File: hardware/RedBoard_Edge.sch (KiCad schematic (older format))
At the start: 67 parts, among them IC3 LM1117, J1 CONN_025MM, J17 Qwiic_Connector, J18 Qwiic_Connector, J2 ICSP, J3 POWER_JACKSUPER_BOMB_DIGITY, J4 microB, J5 CONN_04, J6 CONN_04, Q1 1A/60V/500mO, Q2 MOSFET-NCH-BSS138, Q3 MOSFET-NCH-BSS138, U1 CH340G, U2 MIC5205, U3 Standoff_Grounding, U4 ATMEGA328P_TQFP, U5 Standoff_Grounding, Y1 16MHz, Y2 12MHz

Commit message: conversion to Reds, all parts now point to KiCad library in directory C:/Github
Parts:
- removed C1, C2, C4, C8: 0.1uF, RedBoard:SPARKFUN-CAPACITORS_0603, symbol SPARKFUN-CAPACITORS_0.1UF-0603-25V-_+80_-20%_
- removed C10, C9: 10pF, Capacitors_SMD:C_0603, symbol C_Small
- removed C11: 10nF, Capacitors_SMD:C_0603, symbol C_Small
- removed C12: 0.1uF, Capacitors_SMD:C_0603, symbol C_Small
- removed C3, C6: 10uF, RedBoard:SPARKFUN-CAPACITORS_EIA3216, symbol SPARKFUN-CAPACITORS_10UF-POLAR-EIA3216-16V-10%_TANT_
- removed C5: 47uF, RedBoard:SPARKFUN-CAPACITORS_PANASONIC_D, symbol SPARKFUN-CAPACITORS_47UF-POLAR-PANASONIC_D-35V-20%
- removed C7: 1.0uF, RedBoard:SPARKFUN-CAPACITORS_0603, symbol SPARKFUN-CAPACITORS_1.0UF-0603-16V-10%
- removed D1: MBRA140, RedBoard:SPARKFUN-DISCRETESEMI_SMA-DIODE, symbol SPARKFUN-DISCRETESEMI_MBRA140
- removed D2: Green, NewParts:LED_RED_T1-.75_RT_ANG_PCB, symbol SPARKFUN-LED_LED-GREEN0603
- removed D3: Yellow, NewParts:LED_RED_T1-.75_RT_ANG_PCB, symbol SPARKFUN-LED_LED-YELLOW0603
- removed D4: Red, NewParts:LED_RED_T1-.75_RT_ANG_PCB, symbol SPARKFUN-LED_LED-YELLOW0603
- removed D5: Blue, NewParts:LED_RED_T1-.75_RT_ANG_PCB, symbol SPARKFUN-LED_LED-YELLOW0603
- removed F1: SPARKFUN-FUSES_PTC-HALF_AMP, RedBoard:SPARKFUN-FUSES_1206, symbol SPARKFUN-FUSES_PTC-HALF_AMP
- removed IC3: LM1117, RedBoard:TESTING_SOT223-ALT1, symbol TESTING_V_REG_LM1117ALT1
- removed J17, J18: Qwiic_Connector, SparkX:SparkX-1X04_1MM_RA, symbol Qwiic_Connector
- removed J2: ICSP, RedBoard:SPARKFUN-CONNECTORS_2X3_SMT_POSTS, symbol SPARKFUN-CONNECTORS_AVR_SPI_PROG_3X2SMD
- removed J3: POWER_JACKSUPER_BOMB_DIGITY, RedBoard:TESTING_POWER_JACK_SMD_OVERPASTE_SUPER_BOMB_DIGITY, symbol TESTING_POWER_JACKSUPER_BOMB_DIGITY
- removed J4: microB, Connectors:USB-B-MICRO-SMD, symbol microB
- removed JP1, JP2: JUMPER-SMT_2_NO_SILK, Jumpers:SMT-JUMPER_2_NO_SILK, symbol JUMPER-SMT_2_NO_SILK
- removed JP4, JP6: STAND-OFF, RedBoard:SPARKFUN_STAND-OFF, symbol SPARKFUN_STAND-OFF
- removed JP8, JP9: FIDUCIAL1X2, RedBoard:SPARKFUN_FIDUCIAL-1X2, symbol SPARKFUN_FIDUCIAL1X2
- removed Q1: 1A/60V/500mO, RedBoard:SPARKFUN-DISCRETESEMI_SOT23-3, symbol SPARKFUN-DISCRETESEMI_MOSFET-PCH-ZXMP6A13F
- removed R1: 1k, RedBoard:SPARKFUN-RESISTORS_0603, symbol SPARKFUN-RESISTORS_1KOHM-0603-1_10W-1%
- removed R10, R7, R8, R9: 4.7k, RedBoard:SPARKFUN-RESISTORS_0603, symbol SPARKFUN-RESISTORS_10KOHM-0603-1_10W-1%
- removed R14: 715, RedBoard:SPARKFUN-RESISTORS_0603, symbol SPARKFUN-RESISTORS_715OHM-0603-1_10W-1%
- removed R15: 240, RedBoard:SPARKFUN-RESISTORS_0603, symbol SPARKFUN-RESISTORS_240OHM-0603-1_10W-1%
- removed R2: 1k, RedBoard:SPARKFUN-RESISTORS_0603, symbol SPARKFUN-RESISTORS_4.7KOHM-0603-1_10W-1%
- removed R3, R4: 10k, RedBoard:SPARKFUN-RESISTORS_0603, symbol SPARKFUN-RESISTORS_10KOHM-0603-1_10W-1%
- removed R5, R6: 1k, RedBoard:SPARKFUN-RESISTORS_0603, symbol R_Small
- removed S1: RESET, NewParts:SWITCH_TACTILE_SPST-NO_0.05A_12V, symbol SPARKFUN-ELECTROMECHANICAL_SWITCH_SPST_4_PINSQUARE
- removed S2: SWITCH-SPDT-PTH-11.6X4.0MM, NewParts:RockerSwitch_RA, symbol SWITCH-SPDT-PTH-11.6X4.0MM
- removed U$1: SPARKX-LOGO5, SparkX:SparkX-SPARKX-LARGE, symbol SPARKX_SPARKX-LOGO5
- removed U1: CH340G, IC:SO16, symbol SPARKFUN-DIGITALIC_CH340GSMD
- removed U2: MIC5205, RedBoard:SPARKFUN-POWERIC_SOT23-5, symbol SPARKFUN-POWERIC_MIC52053.3V
- removed U4: ATMEGA328P_TQFP, RedBoard:SPARKFUN-IC-MICROCONTROLLER_TQFP32-08, symbol SPARKFUN-IC-MICROCONTROLLER_ATMEGA328P_TQFP
- removed Y1: 16MHz, RedBoard:SPARKFUN-CLOCKS_RESONATOR-SMD-3.2X1.3, symbol SPARKFUN-CLOCKS_RESONATOR-16MHZSMD_3.2X1.3
- removed Y2: 12MHz, Clocks:CRYSTAL-SMD-3.2X2.5MM, symbol CRYSTAL-GROUNDED
- added C1, C12, C2, C4, C8: 0.1UF-0603-25V-_+80_-20%_, 0603, symbol 0.1UF-0603-25V-_+80_-20%_
- added C10, C9: 10PF-0603-50V-5%, 0603, symbol 10PF-0603-50V-5%
- added C11: 10NF-0603-50V-10%, 0603, symbol 10NF-0603-50V-10%
- added C3, C6: 10UF-POLAR-EIA3216-16V-10%_TANT_, EIA3216, symbol 10UF-POLAR-EIA3216-16V-10%_TANT_
- added C5: 47UF-POLAR-EIA3528-10V-10%, EIA3528, symbol 47UF-POLAR-EIA3528-10V-10%
- added C7: 1.0UF-0603-16V-10%, 0603, symbol 1.0UF-0603-16V-10%
- added D1: DIODE-SHOTTKY_MBRA140, Silicon-Standard:SMA-DIODE, symbol DIODE-SHOTTKY_MBRA140
- added D2, D5: SPARKFUN-LED_LED-YELLOW-550, LED:LED_550_T1-.75_RT_ANG_PCB, symbol SPARKFUN-LED_LED-YELLOW-550
- added D3: SPARKFUN-LED_LED-GREEN-550, LED:LED_550_T1-.75_RT_ANG_PCB, symbol SPARKFUN-LED_LED-GREEN-550
- added D4: SPARKFUN-LED_LED-RED-550, LED:LED_550_T1-.75_RT_ANG_PCB, symbol SPARKFUN-LED_LED-RED-550
- added F1: PPTC_HALF-AMP, 1206, symbol PPTC_HALF-AMP
- added FD1, FD2, FD3, FD4: FIDUCIAL1X2, FIDUCIAL-1X2, symbol FIDUCIAL1X2
- added H1, H2: STAND-OFF, STAND-OFF, symbol STAND-OFF
- added J17, J18: QWIIC_CONNECTORJS-1MM, 1X04_1MM_RA, symbol QWIIC_CONNECTORJS-1MM
- added J2: CONN_03X2SMT, 2X3_SMT_POSTS, symbol CONN_03X2SMT
- added J20: POWER_JACKSMD, POWER_JACK_SMD, symbol POWER_JACKSMD
- added J4: USB_MICRO-B_FEMALE-SMT, USB-B-MICRO-SMD, symbol USB_MICRO-B_FEMALE-SMT
- added JP1, JP2: JUMPER-SMT_2_NO, SMT-JUMPER_2_NO, symbol JUMPER-SMT_2_NO
- added LOGO?: SPARKFUN-AESTHETICS_SFE_LOGO_NAME.1_INCH, symbol SPARKFUN-AESTHETICS_SFE_LOGO_NAME.1_INCH
- added Q1: MOSFET_PCH-SI2309DS, SOT23-3, symbol MOSFET_PCH-SI2309DS
- added R1, R2, R5, R6: 470OHM-0603-1_10W-1%, 0603, symbol 470OHM-0603-1_10W-1%
- added R10, R7, R8, R9: 4.7KOHM-0603-1_10W-1%, 0603, symbol 4.7KOHM-0603-1_10W-1%
- added R14: 715OHM-0603-1_10W-1%, 0603, symbol 715OHM-0603-1_10W-1%
- added R15: 240OHM-0603-1_10W-1%, 0603, symbol 240OHM-0603-1_10W-1%
- added R3, R4: 10KOHM-0603-1_10W-1%, 0603, symbol 10KOHM-0603-1_10W-1%
- added S1: MOMENTARY-SWITCH-SPST-2-PTH-RT-ANGLE, Switches:TACTILE_SWITCH_PTH_RIGHT_ANGLE_KIT, symbol MOMENTARY-SWITCH-SPST-2-PTH-RT-ANGLE
- added S2: ROCKER_SWITCH-SPST_PTH_RIGHT_ANGLE, TACTILE_SWITCH_SMD_RIGHT_ANGLE, symbol ROCKER_SWITCH-SPST_PTH_RIGHT_ANGLE
- added U1: CH340GSMD, Silicon-Standard:SO16, symbol CH340GSMD
- added U2: V_REG_MIC52053.3V, SOT23-5, symbol V_REG_MIC52053.3V
- added U4: ATMEGA328P_TQFP, TQFP32-08, symbol ATMEGA328P_TQFP
- added U6: V_REG_LM1117SOT223, SOT223, symbol V_REG_LM1117SOT223
- added Y1: RESONATOR-16MHZSMD_3.2X1.3, RESONATOR-SMD-3.2X1.3, symbol RESONATOR-16MHZSMD_3.2X1.3
- added Y2: CRYSTAL-12MHZ\", CRYSTAL-SMD-5X3.2-4PAD, symbol CRYSTAL-12MHZ"
- 5V1, ADC1, GND1: footprint Connectors:1X06 -> 1X06; Field4 (none) -> CONN-08437
- 5V2, 5V3, GND2, GND3, J5, J6, PWM1, SPI1: footprint Connectors:1X04 -> 1X04; Field4 (none) -> CONN-09696
- J1: footprint Connectors:SCREWTERMINAL-5MM-2 -> SCREWTERMINAL-5MM-2; Field4 (none) -> PRT-08432
- Q2, Q3: footprint DiscreteSemi:SparkFun-DiscreteSemi-SOT23-3 -> SOT23-3; Field4 (none) -> TRANS-00830
- U3, U5: footprint NewParts:Standoff_Grounding -> Hardware:STANDOFF_GROUNDING
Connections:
- wire segments 250 -> 246

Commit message: Conversion to Reds
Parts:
- added J3, J7, J8: CONN_02, symbol CONN_02
- 5V1, ADC1, GND1: footprint 1X06 -> (none)
- 5V2, 5V3, GND2, GND3, J5, J6, PWM1, SPI1: footprint 1X04 -> (none)
- C1, C10, C11, C12, C2, C4, C7, C8, C9: footprint 0603 -> Capacitors:0603
- C3, C6: footprint EIA3216 -> Capacitors:EIA3216
- C5: footprint EIA3528 -> Capacitors:EIA3528
- F1: footprint 1206 -> Fuses:1206
- FD1, FD2, FD3, FD4: footprint FIDUCIAL-1X2 -> Aesthetics:FIDUCIAL-MICRO
- H1, H2: footprint STAND-OFF -> Hardware:STAND-OFF-TIGHT
- J1: footprint SCREWTERMINAL-5MM-2 -> (none)
- J17, J18: footprint 1X04_1MM_RA -> (none)
- J2: footprint 2X3_SMT_POSTS -> (none)
- J20: footprint POWER_JACK_SMD -> (none)
- J4: footprint USB-B-MICRO-SMD -> (none)
- JP1, JP2: footprint SMT-JUMPER_2_NO -> Jumpers:SMT-JUMPER_2_NO_NO-SILK
- Q1, Q2, Q3: footprint SOT23-3 -> Silicon-Standard:SOT23-3
- R1, R10, R14, R15, R2, R3, R4, R5, R6, R7, R8, R9: footprint 0603 -> Resistors:0603
- S2: footprint TACTILE_SWITCH_SMD_RIGHT_ANGLE -> Switches:TACTILE_SWITCH_SMD_RIGHT_ANGLE
- U2: footprint SOT23-5 -> Silicon-Standard:SOT23-5
- U4: footprint TQFP32-08 -> Silicon-Standard:TQFP32-08
- U6: footprint SOT223 -> Silicon-Standard:SOT223
- Y1: footprint RESONATOR-SMD-3.2X1.3 -> Clocks:RESONATOR-SMD-3.2X1.3
- Y2: footprint CRYSTAL-SMD-5X3.2-4PAD -> Clocks:CRYSTAL-SMD-5X3.2-4PAD

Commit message: Post Design review changes
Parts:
- removed 5V1, ADC1, GND1: CONN_06SILK_FEMALE_PTH, symbol CONN_06SILK_FEMALE_PTH
- removed J18: QWIIC_CONNECTORJS-1MM, symbol QWIIC_CONNECTORJS-1MM
- removed J3, J7, J8: CONN_02, symbol CONN_02
- added 5V1, 5V4, ADC1, ADC4, GND1, GND4: CONN_04, Connectors:1X04_NO_SILK, symbol CONN_04
- 5V2, 5V3, GND2, GND3: footprint (none) -> Connectors:1X04_NO_SILK
- C1, C10, C11, C12, C2, C4, C7, C8, C9: footprint Capacitors:0603 -> (none)
- C3, C6: footprint Capacitors:EIA3216 -> (none)
- C5: footprint Capacitors:EIA3528 -> (none)
- D1: footprint Silicon-Standard:SMA-DIODE -> (none)
- D2, D3, D4, D5: footprint LED:LED_550_T1-.75_RT_ANG_PCB -> (none)
- F1: footprint Fuses:1206 -> (none)
- FD1, FD2, FD3, FD4: footprint Aesthetics:FIDUCIAL-MICRO -> (none)
- H1, H2: footprint Hardware:STAND-OFF-TIGHT -> (none)
- J20: footprint (none) -> Connectors:POWER_JACK_SMD_GND
- JP1, JP2: footprint Jumpers:SMT-JUMPER_2_NO_NO-SILK -> (none)
- Q1, Q2, Q3: footprint Silicon-Standard:SOT23-3 -> (none)
- R1, R10, R14, R15, R2, R3, R4, R5, R6, R7, R8, R9: footprint Resistors:0603 -> (none)
- S1: footprint Switches:TACTILE_SWITCH_PTH_RIGHT_ANGLE_KIT -> (none)
- S2: footprint Switches:TACTILE_SWITCH_SMD_RIGHT_ANGLE -> (none)
- U1: footprint Silicon-Standard:SO16 -> (none)
- U2: footprint Silicon-Standard:SOT23-5 -> (none)
- U3, U5: footprint Hardware:STANDOFF_GROUNDING -> (none)
- U4: footprint Silicon-Standard:TQFP32-08 -> (none)
- U6: footprint Silicon-Standard:SOT223 -> (none)
- Y1: footprint Clocks:RESONATOR-SMD-3.2X1.3 -> (none)
- Y2: footprint Clocks:CRYSTAL-SMD-5X3.2-4PAD -> (none)
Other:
- moved on the sheet: S2

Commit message: forgot to save before commit
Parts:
- added LOGO1: SFE_LOGO_NAME_FLAME.1_INCH, SFE_LOGO_NAME_FLAME_.1, symbol SFE_LOGO_NAME_FLAME.1_INCH
- added LOGO2: OSHW-LOGOS, OSHW-LOGO-S, symbol OSHW-LOGOS
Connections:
- wire segments 246 -> 247
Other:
- note added: "Design by: Nick Poole"
- note added: "Revised by: Andy England"
- note added: "v01"

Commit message: QC Double Check Issues
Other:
- note added: "The Standoffs on the left side"
- note added: "of the board can be connected"
- note added: "or the board ground by connecting"
- note added: "their respective jumpers."
- note added: "to the grounds for the USB shield"
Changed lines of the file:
@@
 Text Notes 15950 10350 0    50   ~ 0
 v01
+Text Notes 6200 6050 0    50   ~ 0
+The Standoffs on the left side
+Text Notes 6200 6100 0    50   ~ 0
+of the board can be connected
+Text Notes 6150 6150 0    50   ~ 0
+ to the grounds for the USB shield
+Text Notes 6200 6200 0    50   ~ 0
+or the board ground by connecting
+Text Notes 6200 6250 0    50   ~ 0
+their respective jumpers.
 $EndSCHEMATC

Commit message: Post double double check changes
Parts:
- removed LOGO?: SPARKFUN-AESTHETICS_SFE_LOGO_NAME.1_INCH, symbol SPARKFUN-AESTHETICS_SFE_LOGO_NAME.1_INCH
- J1: footprint (none) -> SCREWTERMINAL-5MM-2; Field4 PRT-08432 -> CONN-10480
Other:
- note added: "The Qwiic system operates at 3.3V.\nThe regular I2C pins on the board operate at 5V"

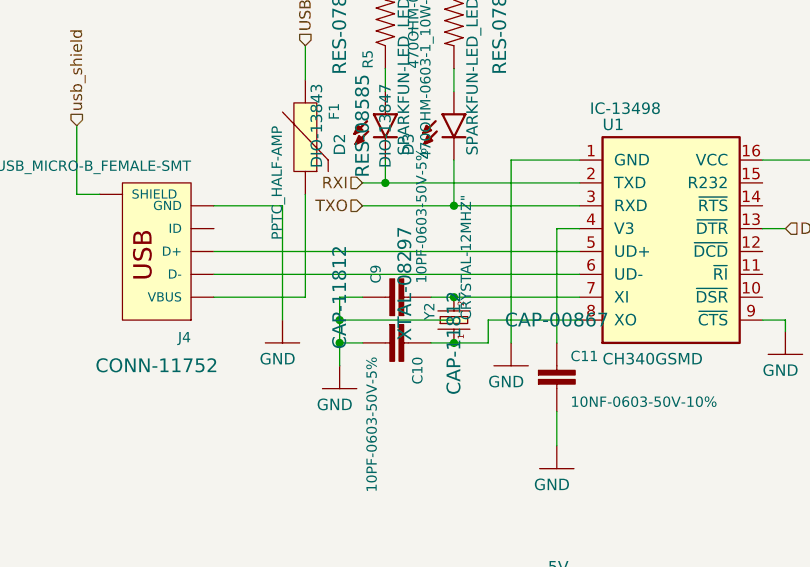
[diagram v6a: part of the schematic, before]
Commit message: updated 12mhz crystal
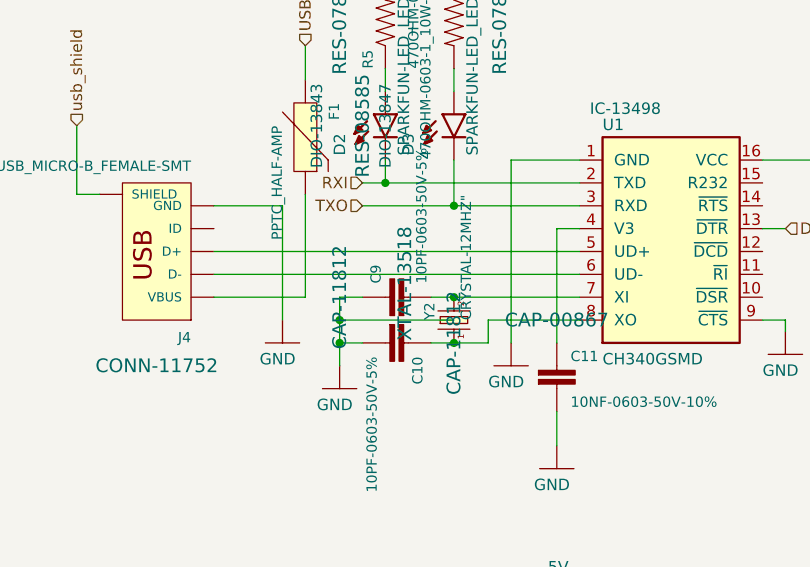
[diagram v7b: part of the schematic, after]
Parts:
- Y2: footprint (none) -> CRYSTAL-SMD-5X3.2-4PAD; Field4 XTAL-08297 -> XTAL-13518
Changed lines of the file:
@@
-$EndComp
-$Comp
-L CRYSTAL-12MHZ" Y2
-U 1 1 59F02843
-P 2950 3000
-F 0 "Y2" H 2950 3080 45  0000 L BNN
-F 1 "CRYSTAL-12MHZ\"" H 2950 2920 45  0000 L BNN
-F 2 "" H 2980 3150 20  0001 C CNN
-F 3 "" H 2950 3000 50  0001 C CNN
-F 4 "XTAL-08297" H 3110 3215 60  0000 C CNN "Field4"
-	1    2950 3000
-	0    -1   -1   0
 $EndComp
 $Comp
@@
 Text Notes 12200 6050 0    50   ~ 0
 The Qwiic system operates at 3.3V.\nThe regular I2C pins on the board operate at 5V
+$Comp
+L CRYSTAL-12MHZ" Y2
+U 1 1 5A382753
+P 2950 3000
+F 0 "Y2" H 2950 3080 45  0000 L BNN
+F 1 "CRYSTAL-12MHZ\"" H 2950 2920 45  0000 L BNN
+F 2 "CRYSTAL-SMD-5X3.2-4PAD" H 2980 3150 20  0001 C CNN
+F 3 "" H 2950 3000 50  0001 C CNN
+F 4 "XTAL-13518" H 3110 3215 60  0000 C CNN "Field4"
+	1    2950 3000
+	0    -1   -1   0
+$EndComp
 $EndSCHEMATC

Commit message: v02
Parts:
- removed C5: 47UF-POLAR-EIA3528-10V-10%, symbol 47UF-POLAR-EIA3528-10V-10%
- added C5: 47UF-POLAR-PANASONIC_D-35V-20%, Capacitors:PANASONIC_D, symbol 47UF-POLAR-PANASONIC_D-35V-20%
- C1, C10, C11, C12, C2, C4, C7, C8, C9: footprint (none) -> Capacitors:0603
- C3, C6: footprint (none) -> Capacitors:EIA3216
- D1: footprint (none) -> Silicon-Standard:SMA-DIODE
- D2, D3, D4, D5: footprint (none) -> LED:LED_550_T1-.75_RT_ANG_PCB
- F1: footprint (none) -> Fuses:1206
- FD1, FD2, FD3, FD4: footprint (none) -> Aesthetics:FIDUCIAL-1X2
- H1, H2: footprint (none) -> Hardware:STAND-OFF
- J1: footprint SCREWTERMINAL-5MM-2 -> Connectors:SCREWTERMINAL-5MM-2
- J17: footprint (none) -> Connectors:1X04_1MM_RA
- J2: footprint (none) -> Connectors:2X3-NS
- J4: footprint (none) -> Connectors:USB-B-MICRO-SMD
- J5, J6, PWM1, SPI1: footprint (none) -> Connectors:1X04_NO_SILK
- JP1, JP2: footprint (none) -> Jumpers:SMT-JUMPER_2_NO_NO-SILK
- LOGO1: footprint SFE_LOGO_NAME_FLAME_.1 -> Aesthetics:SFE_LOGO_NAME_FLAME_.1
- LOGO2: footprint OSHW-LOGO-S -> Aesthetics:OSHW-LOGO-S
- Q1, Q2, Q3: footprint (none) -> Silicon-Standard:SOT23-3
- R1, R10, R14, R15, R2, R3, R4, R5, R6, R7, R8, R9: footprint (none) -> Resistors:0603
- S1: footprint (none) -> Switches:SWITCH TACTILE SPST-NO 0.05A 12V
- S2: footprint (none) -> Switches:RockerSwitch_RA
- U1: footprint (none) -> Silicon-Standard:SO16
- U2: footprint (none) -> Silicon-Standard:SOT23-5
- U3, U5: footprint (none) -> Hardware:STANDOFF_GROUNDING
- U4: footprint (none) -> Silicon-Standard:TQFP32-08
- U6: footprint (none) -> Silicon-Standard:SOT223
- Y1: footprint (none) -> Clocks:RESONATOR-SMD-3.2X1.3
- Y2: footprint CRYSTAL-SMD-5X3.2-4PAD -> Clocks:CRYSTAL-SMD-5X3.2-4PAD
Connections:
- net GND: now also J20.P$4 (GND), Q1.1 (G), R4.1, C5.-
- net SCK: now also U4.17 (PB5(SCK))
- net VIN: now also C5.+
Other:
- note added: "v02"
- note removed: "v01"
